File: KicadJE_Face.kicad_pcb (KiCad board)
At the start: 2 copper layers, 40 x 128 mm, 14 parts

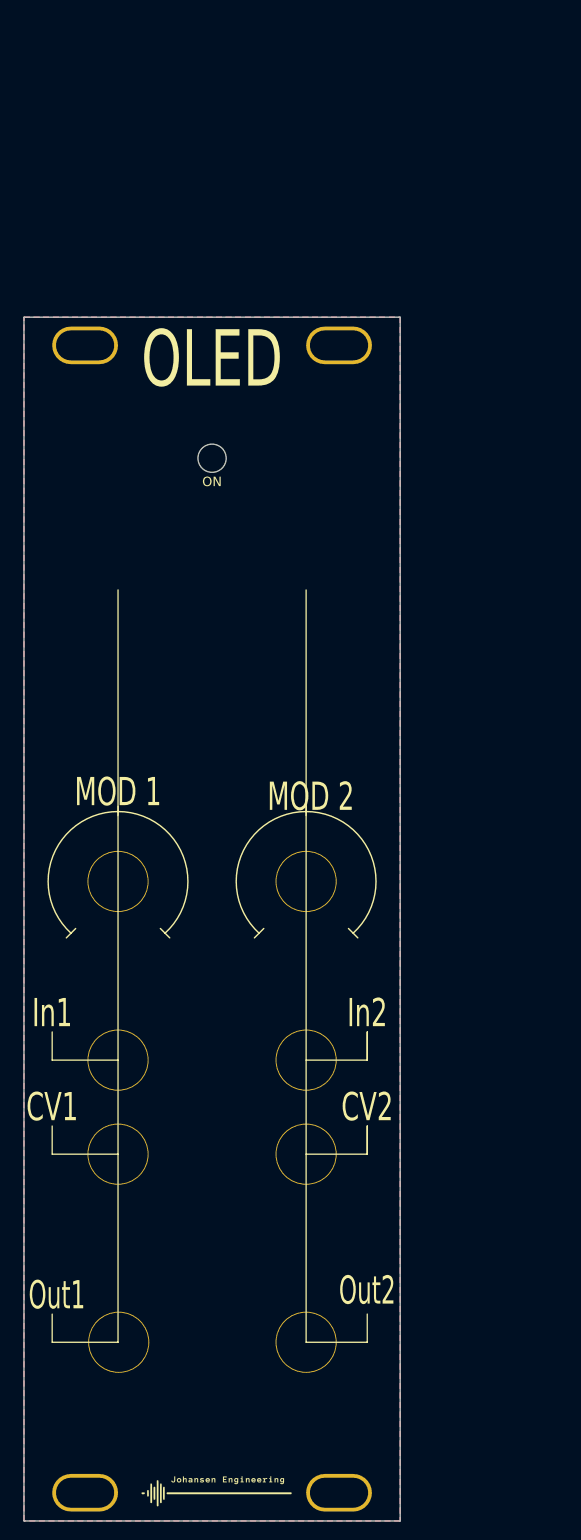
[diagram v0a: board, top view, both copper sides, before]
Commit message: Mouting holes to pads - DRC
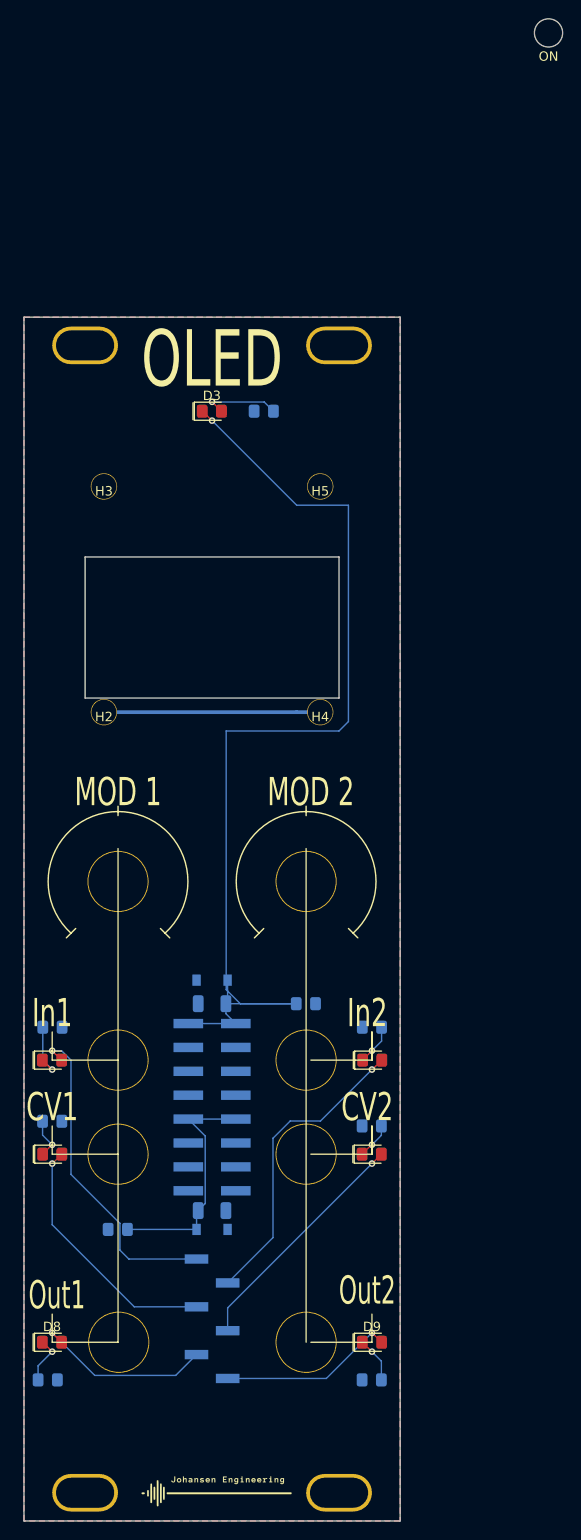
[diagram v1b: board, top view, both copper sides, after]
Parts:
- removed H101: ON, AJ:LED_Hole_3mm
- added C1: 1u, Capacitor_SMD:C_1206_3216Metric, B.Cu at (213.0, 131.0)
- added C2: 1u, Capacitor_SMD:C_1206_3216Metric, B.Cu at (213.0, 109.0)
- added C3: 100n, AJ:C_0805_AJ, B.Cu at (203.0, 133.0)
- added C4: 100n, AJ:C_0805_AJ, B.Cu at (223.0, 109.0)
- added D1: 1N1007, Diode_SMD:D_SOD-123, B.Cu at (213.0, 133.0)
- added D2: 1N1007, Diode_SMD:D_SOD-123, B.Cu at (213.0, 106.5)
- added D3: LED, AJ:D_0805_AJ, F.Cu at (213.0, 46.0)
- added D4: LED, AJ:D_0805_AJ, F.Cu at (196.0, 115.0)
- added D5: LED, AJ:D_0805_AJ, F.Cu at (230.0, 115.0)
- added D6: LED, AJ:D_0805_AJ, F.Cu at (196.0, 125.0)
- added D7: LED, AJ:D_0805_AJ, F.Cu at (230.0, 125.0)
- added D8: LED, AJ:D_0805_AJ, F.Cu at (196.0, 145.0)
- added D9: LED, AJ:D_0805_AJ, F.Cu at (230.0, 145.0)
- added H1: ON, AJ:LED_Hole_3mm, F.Cu at (248.8, 5.78)
- added H2: OLED, AJ:M2.7_Plated, F.Cu at (201.5, 78.0)
- added H3: OLED, AJ:M2.7_Plated, F.Cu at (201.5, 54.0)
- added H4: OLED, AJ:M2.7_Plated, F.Cu at (224.5, 78.0)
- added H5: OLED, AJ:M2.7_Plated, F.Cu at (224.5, 54.0)
- added J1: LED 1-6, Connector_PinHeader_2.54mm:PinHeader_1x06_P2.54mm_Vertical_SMD_Pin1Right, B.Cu at (213.0, 142.5)
- added P1: Doepfer_Power_16pin, Connector_PinHeader_2.54mm:PinHeader_2x08_P2.54mm_Vertical_SMD, B.Cu at (213.0, 120.0)
- added R1: 22k, AJ:R_0805_AJ, B.Cu at (218.5, 46.0)
- added R2: 12k, AJ:R_0805_AJ, B.Cu at (196.0, 111.5)
- added R3: 12k, AJ:R_0805_AJ, B.Cu at (230.0, 111.5)
- added R4: 12k, AJ:R_0805_AJ, B.Cu at (196.0, 121.5)
- added R5: 12k, AJ:R_0805_AJ, B.Cu at (230.0, 122.0)
- added R6: 12k, AJ:R_0805_AJ, B.Cu at (195.5, 149.0)
- added R7: 12k, AJ:R_0805_AJ, B.Cu at (230.0, 149.0)
- renumbered H103 to H6, H102 to H7, H105 to H8, H104 to H9
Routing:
- net -12VA: track 0.00 -> 109.3 mm, vias 0 -> 1
- net Net-(D4-Pad2): track 0.00 -> 34.7 mm, vias 0 -> 1
- net Net-(D5-Pad2): track 0.00 -> 32.4 mm, vias 0 -> 1
- net Net-(D6-Pad2): track 0.00 -> 26.9 mm, vias 0 -> 1
- net Net-(D7-Pad2): track 0.00 -> 25.5 mm, vias 0 -> 1
- net +12VA: track 0.00 -> 25.3 mm
- net GND: track 0.00 -> 23.0 mm
- net Net-(D8-Pad2): track 0.00 -> 19.6 mm, vias 0 -> 1
- net Net-(D9-Pad2): track 0.00 -> 18.8 mm, vias 0 -> 1
- net Net-(D3-Pad2): track 0.00 -> 8.35 mm, vias 0 -> 1
- net Net-(D4-Pad1): track 0.00 -> 6.38 mm, vias 0 -> 1
- net Net-(D8-Pad1): track 0.00 -> 5.09 mm, vias 0 -> 1
- net Net-(D9-Pad1): track 0.00 -> 4.85 mm, vias 0 -> 1
- net Net-(D6-Pad1): track 0.00 -> 4.36 mm, vias 0 -> 1
- net Net-(D5-Pad1): track 0.00 -> 4.34 mm, vias 0 -> 1
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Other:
- outline, holes or cut-outs redrawn

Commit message: Gerber
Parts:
- removed H1: ON, AJ:LED_Hole_3mm
